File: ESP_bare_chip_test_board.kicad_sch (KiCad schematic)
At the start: 0 parts

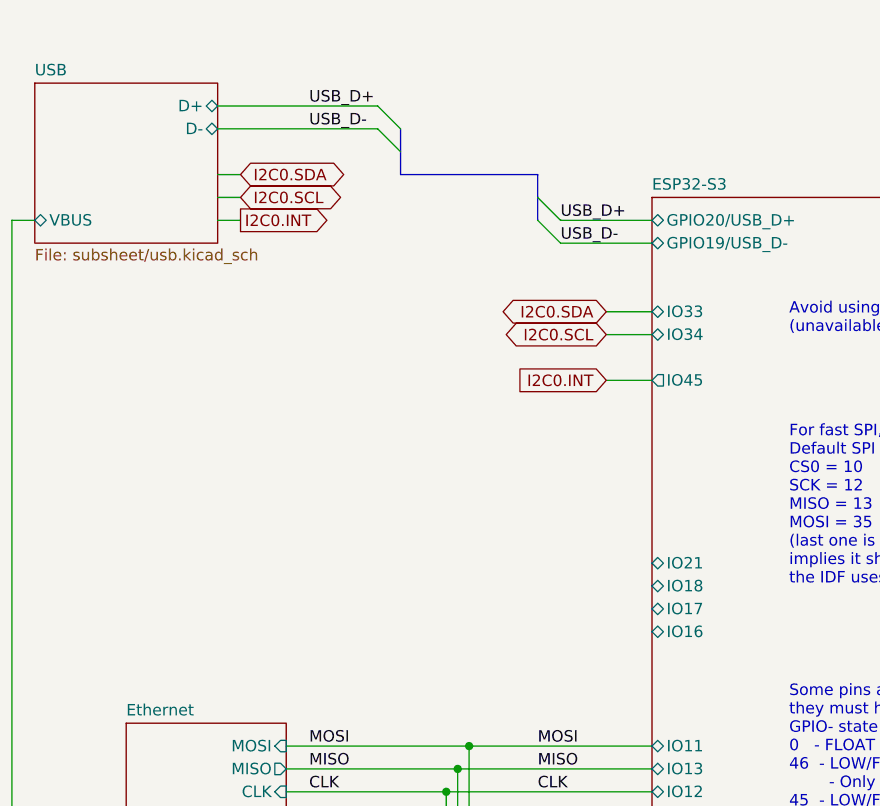
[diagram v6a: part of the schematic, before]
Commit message: Wire remaining traces, fix DRC errors
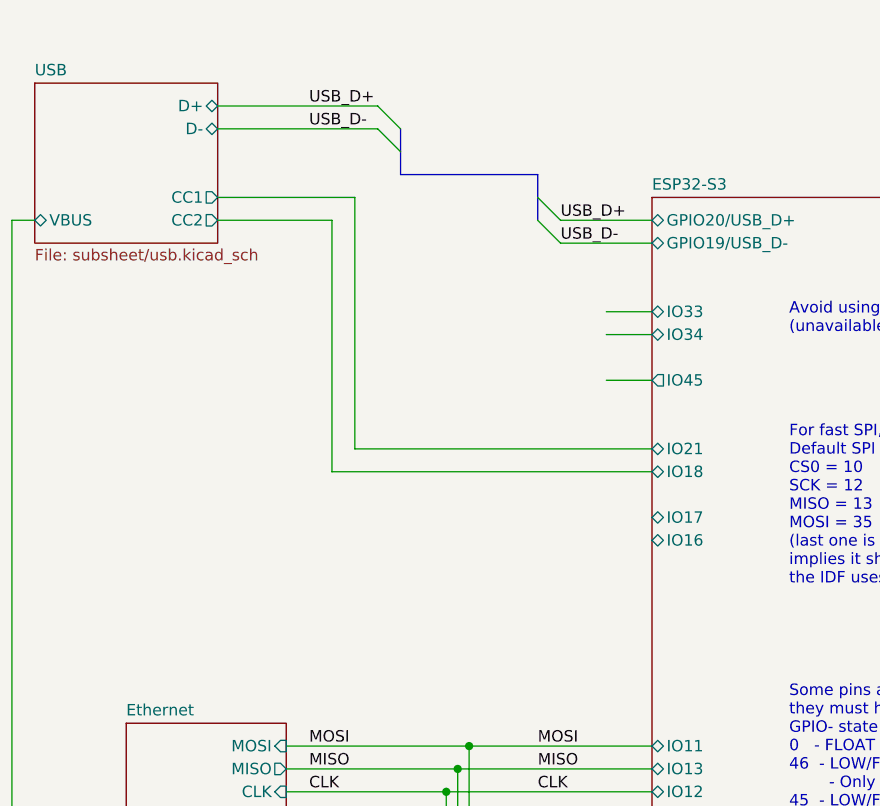
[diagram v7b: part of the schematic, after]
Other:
- sheet USB ports: added CC1, CC2; removed none
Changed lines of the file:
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@@
+	(wire
+		(pts
+			(xy 53.34 30.48) (xy 38.1 30.48)
+		)
+		(stroke
+			(width 0)
+			(type default)
+		)
+	)
+	(wire
+		(pts
+			(xy 50.8 33.02) (xy 50.8 60.96)
+		)
+		(stroke
+			(width 0)
+			(type default)
+		)
+	)
 	(wire
 		(pts
@@
 	(wire
 		(pts
+			(xy 38.1 33.02) (xy 50.8 33.02)
+		)
+		(stroke
+			(width 0)
+			(type default)
+		)
+	)
+	(wire
+		(pts
 			(xy 198.12 114.3) (xy 238.76 114.3)
 		)
@@
 	(wire
 		(pts
+			(xy 53.34 58.42) (xy 53.34 30.48)
+		)
+		(stroke
+			(width 0)
+			(type default)
+		)
+	)
+	(wire
+		(pts
+			(xy 50.8 60.96) (xy 86.36 60.96)
+		)
+		(stroke
+			(width 0)
+			(type default)
+		)
+	)
+	(wire
+		(pts
+			(xy 86.36 58.42) (xy 53.34 58.42)
+		)
+		(stroke
+			(width 0)
+			(type default)
+		)
+	)
+	(wire
+		(pts
 			(xy 45.72 96.52) (xy 63.5 96.52)
 		)
@@
 	(wire
 		(pts
-			(xy 38.1 27.94) (xy 40.64 27.94)
-		)
-		(stroke
-			(width 0)
-			(type default)
-		)
-	)
-	(wire
-		(pts
 			(xy 160.02 53.34) (xy 167.64 53.34)
 		)
@@
 	(wire
 		(pts
-			(xy 38.1 33.02) (xy 40.64 33.02)
-		)
-		(stroke
-			(width 0)
-			(type default)
-		)
-	)
-	(wire
-		(pts
 			(xy 38.1 20.32) (xy 55.88 20.32)
 		)
@@
 		(pts
 			(xy 66.04 121.92) (xy 66.04 134.62)
-		)
-		(stroke
-			(width 0)
-			(type default)
-		)
-	)
-	(wire
-		(pts
-			(xy 38.1 30.48) (xy 40.64 30.48)
 		)
 		(stroke
@@
 			)
 			(justify left bottom)
-		)
-	)
-	(global_label "I2C0.INT"
-		(shape input)
-		(at 81.28 50.8 180)
-		(fields_autoplaced yes)
-		(effects
-			(font
-				(size 1.27 1.27)
-			)
-			(justify right)
-		)
-		(property "Intersheetrefs" "${INTERSHEET_REFS}"
-			(at 70.4933 50.8 0)
-			(effects
-				(font
-					(size 1.27 1.27)
-				)
-				(justify right)
-				(hide yes)
-			)
-		)
-	)
-	(global_label "I2C0.SCL"
-		(shape bidirectional)
-		(at 81.28 45.72 180)
-		(fields_autoplaced yes)
-		(effects
-			(font
-				(size 1.27 1.27)
-			)
-			(justify right)
-		)
-		(property "Intersheetrefs" "${INTERSHEET_REFS}"
-			(at 68.7773 45.72 0)
-			(effects
-				(font
-					(size 1.27 1.27)
-				)
-				(justify right)
-				(hide yes)
-			)
-		)
-	)
-	(global_label "I2C0.INT"
-		(shape output)
-		(at 40.64 33.02 0)
-		(fields_autoplaced yes)
-		(effects
-			(font
-				(size 1.27 1.27)
-			)
-			(justify left)
-		)
-		(property "Intersheetrefs" "${INTERSHEET_REFS}"
-			(at 51.4267 33.02 0)
-			(effects
-				(font
-					(size 1.27 1.27)
-				)
-				(justify left)
-				(hide yes)
-			)
-		)
-	)
-	(global_label "I2C0.SDA"
-		(shape bidirectional)
-		(at 40.64 27.94 0)
-		(fields_autoplaced yes)
-		(effects
-			(font
-				(size 1.27 1.27)
-			)
-			(justify left)
-		)
-		(property "Intersheetrefs" "${INTERSHEET_REFS}"
-			(at 53.2032 27.94 0)
-			(effects
-				(font
-					(size 1.27 1.27)
-				)
-				(justify left)
-				(hide yes)
-			)
-		)
-	)
-	(global_label "I2C0.SDA"
-		(shape bidirectional)
-		(at 81.28 43.18 180)
-		(fields_autoplaced yes)
-		(effects
-			(font
-				(size 1.27 1.27)
-			)
-			(justify right)
-		)
-		(property "Intersheetrefs" "${INTERSHEET_REFS}"
-			(at 68.7168 43.18 0)
-			(effects
-				(font
-					(size 1.27 1.27)
-				)
-				(justify right)
-				(hide yes)
-			)
-		)
-	)
-	(global_label "I2C0.SCL"
-		(shape bidirectional)
-		(at 40.64 30.48 0)
-		(fields_autoplaced yes)
-		(effects
-			(font
-				(size 1.27 1.27)
-			)
-			(justify left)
-		)
-		(property "Intersheetrefs" "${INTERSHEET_REFS}"
-			(at 53.1427 30.48 0)
-			(effects
-				(font
-					(size 1.27 1.27)
-				)
-				(justify left)
-				(hide yes)
-			)
 		)
 	)
@@
 		)
 		(pin "IO17" bidirectional
-			(at 86.36 76.2 180)
+			(at 86.36 66.04 180)
 			(effects
 				(font
@@
 		)
 		(pin "IO18" bidirectional
-			(at 86.36 73.66 180)
+			(at 86.36 60.96 180)
 			(effects
 				(font
@@
 		)
 		(pin "IO21" bidirectional
-			(at 86.36 71.12 180)
+			(at 86.36 58.42 180)
 			(effects
 				(font
@@
 		)
 		(pin "IO16" bidirectional
-			(at 86.36 78.74 180)
+			(at 86.36 68.58 180)
 			(effects
 				(font
@@
 			)
 		)
+		(pin "CC1" output
+			(at 38.1 30.48 0)
+			(effects
+				(font
+					(size 1.27 1.27)
+				)
+				(justify right)
+			)
+		)
+		(pin "CC2" output
+			(at 38.1 33.02 0)
+			(effects
+				(font
+					(size 1.27 1.27)
+				)
+				(justify right)
+			)
+		)

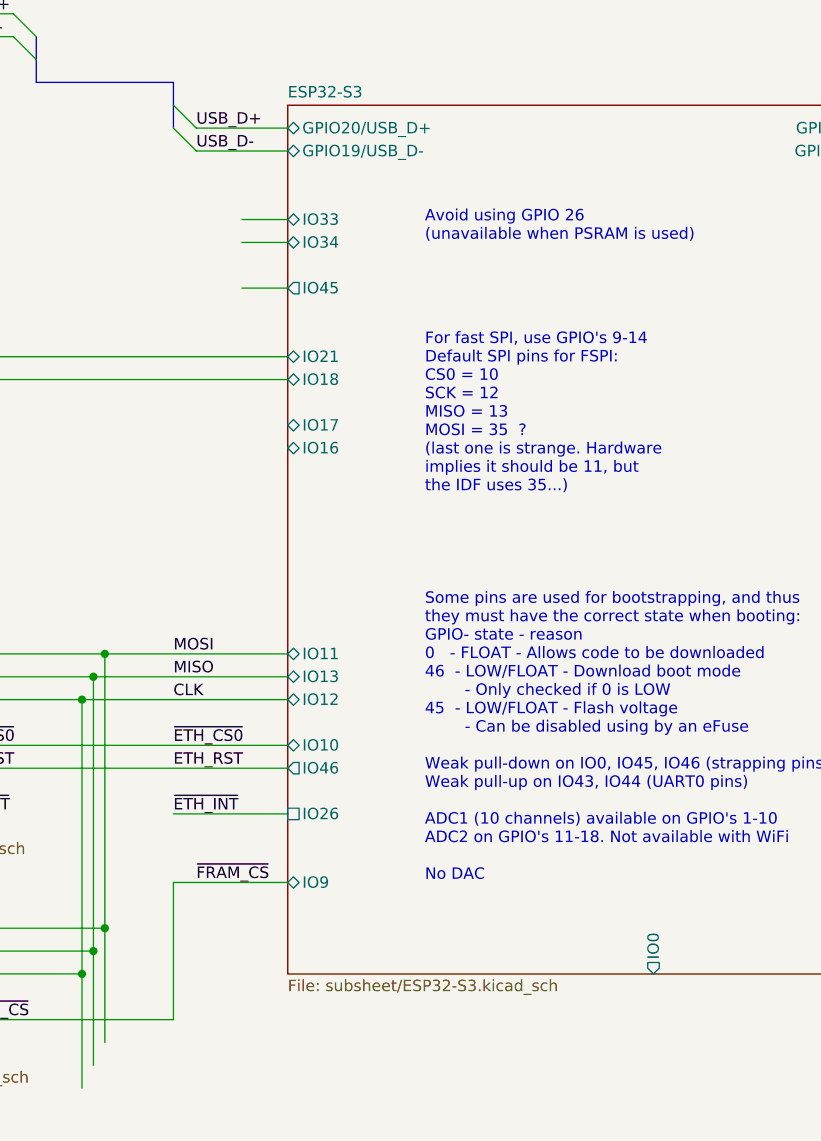
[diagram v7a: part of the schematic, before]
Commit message: Add test pads for extra IO pins
Can be soldered to if desired for some testing purpose
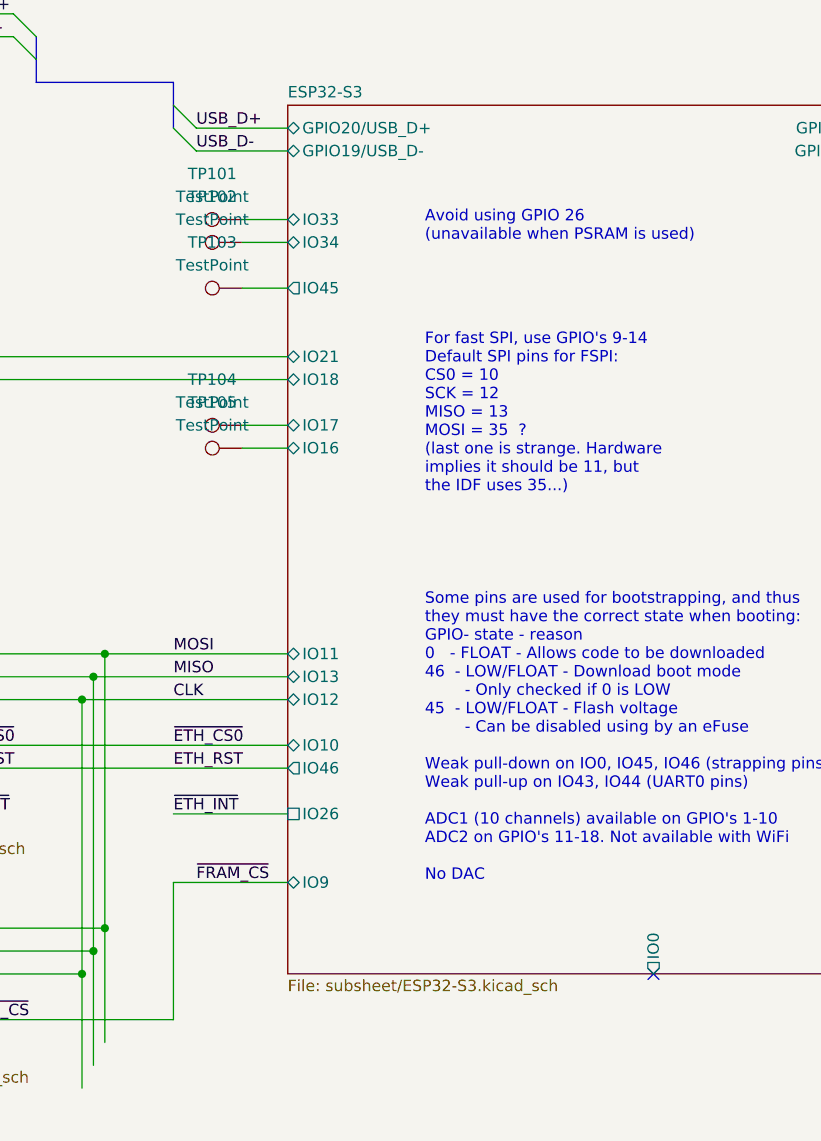
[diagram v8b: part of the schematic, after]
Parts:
- added TP101, TP102, TP103, TP104, TP105: TestPoint, TestPoint:TestPoint_Pad_D2.0mm, symbol Connector:TestPoint
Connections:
- net ESP32-S3/IO16: now also TP105.1
- net ESP32-S3/IO17: now also TP104.1
- net ESP32-S3/IO33: now also TP101.1
- net ESP32-S3/IO34: now also TP102.1
- net ESP32-S3/IO45: now also TP103.1
- no-connect marks 2 -> 3
